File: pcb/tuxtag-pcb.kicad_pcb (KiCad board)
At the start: 2 copper layers, 25.8 x 37.2 mm, 10 parts, among them J1 vibrator, J2 battery, J3 buzzer, Q1 P2N2222A, U1 ESP32-C3_SUPERMINI_TH

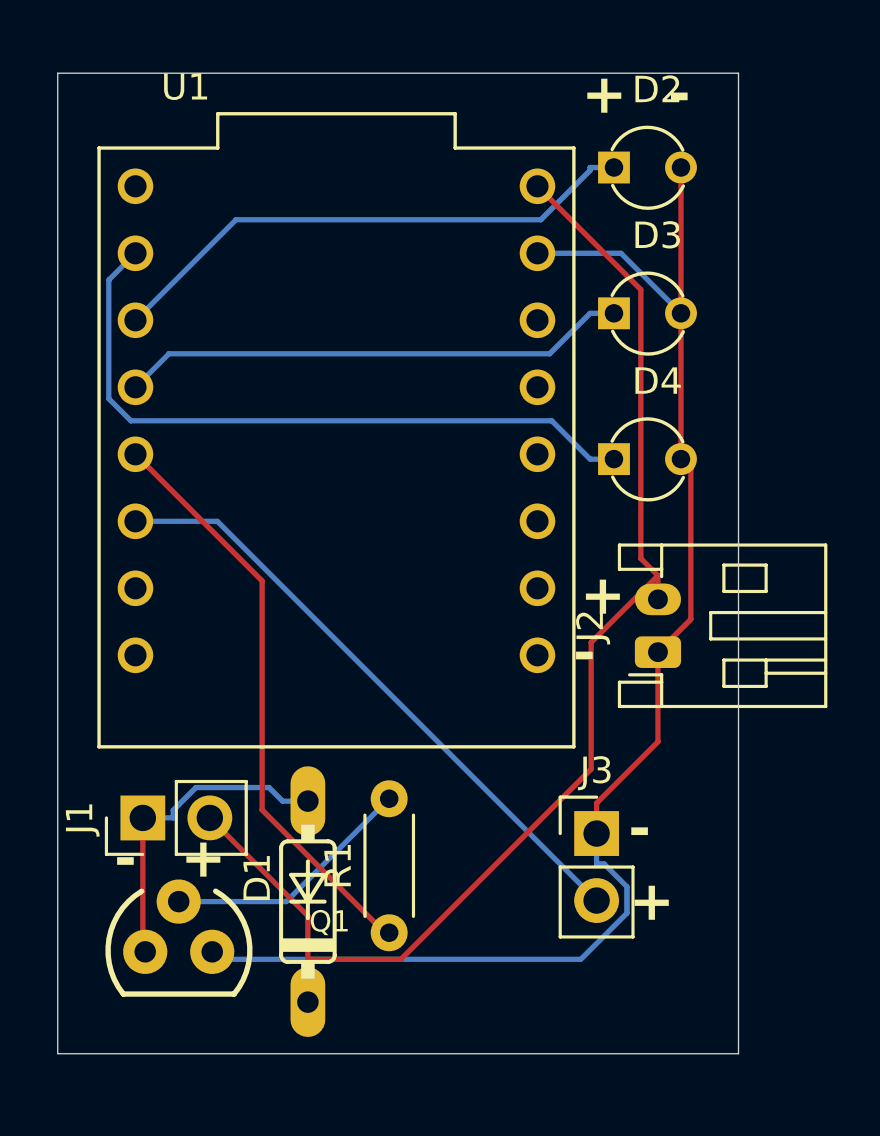
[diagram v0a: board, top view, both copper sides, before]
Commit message: Added resistors to LEDs
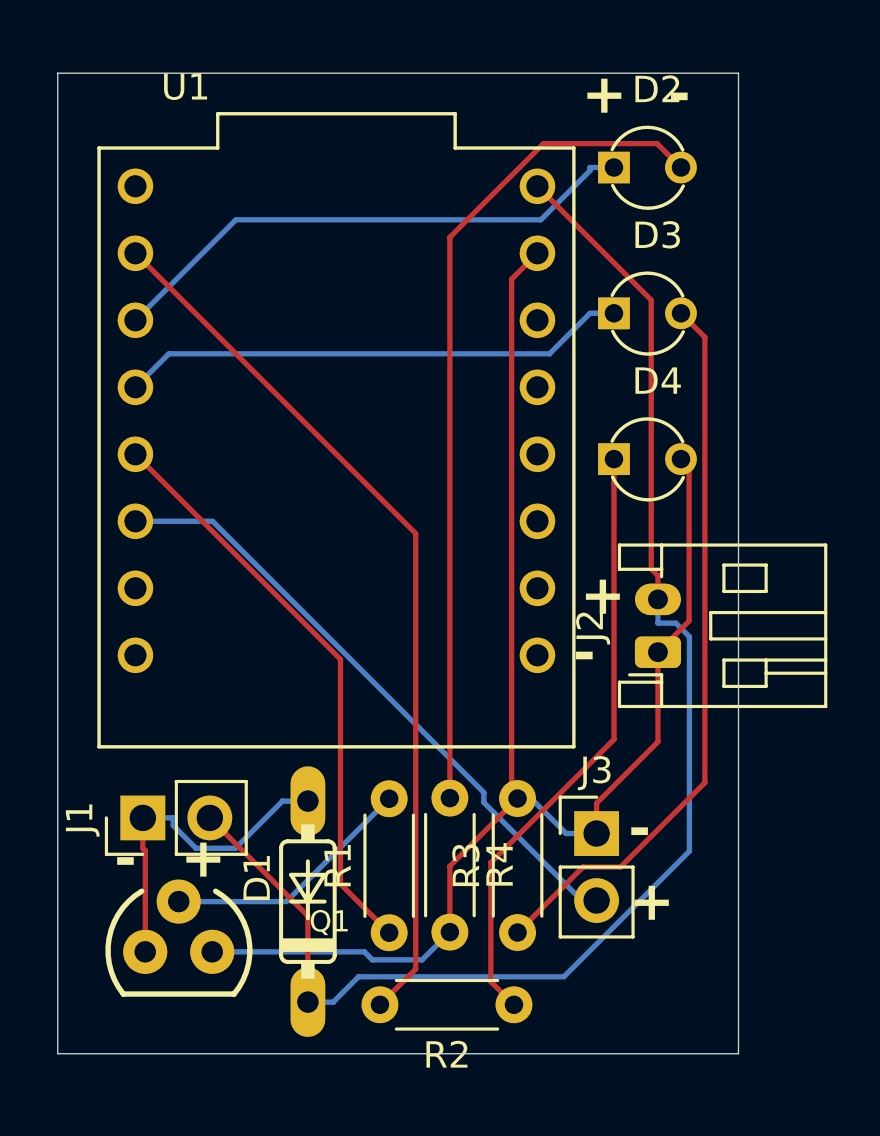
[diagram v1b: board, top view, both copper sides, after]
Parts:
- added R2: R, Resistor_THT:R_Axial_DIN0204_L3.6mm_D1.6mm_P5.08mm_Horizontal, F.Cu at (134.8, 79.2)
- added R3: R, Resistor_THT:R_Axial_DIN0204_L3.6mm_D1.6mm_P5.08mm_Horizontal, F.Cu at (134.9, 76.5)
- added R4: R, Resistor_THT:R_Axial_DIN0204_L3.6mm_D1.6mm_P5.08mm_Horizontal, F.Cu at (132.3, 71.4)
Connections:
- D2 pad C: Net-(J2-Pin_1) -> Net-(D2-PadC)
- D3 pad C: Net-(J2-Pin_1) -> Net-(D3-PadC)
- D4 pad A: Net-(U1-GPIO6) -> Net-(D4-PadA)
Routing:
- net Net-(D2-PadC): track 0.00 -> 31.9 mm
- net Net-(D3-PadC): track 0.00 -> 27.6 mm
- net Net-(D4-PadA): track 0.00 -> 23.0 mm
- net Net-(U1-GPIO6): track 26.0 -> 33.5 mm
- net Net-(J1-Pin_2): track 48.2 -> 53.3 mm
- net Net-(J2-Pin_1): track 53.5 -> 56.2 mm
- net Net-(J1-Pin_1): track 12.2 -> 12.8 mm
